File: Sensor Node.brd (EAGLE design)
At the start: 30.5 x 59.7 mm, 31 parts, among them Q1 IRLML6402, U1 ATMEGA328P_TQFP, X16 16MHZ, X8 8MHZ

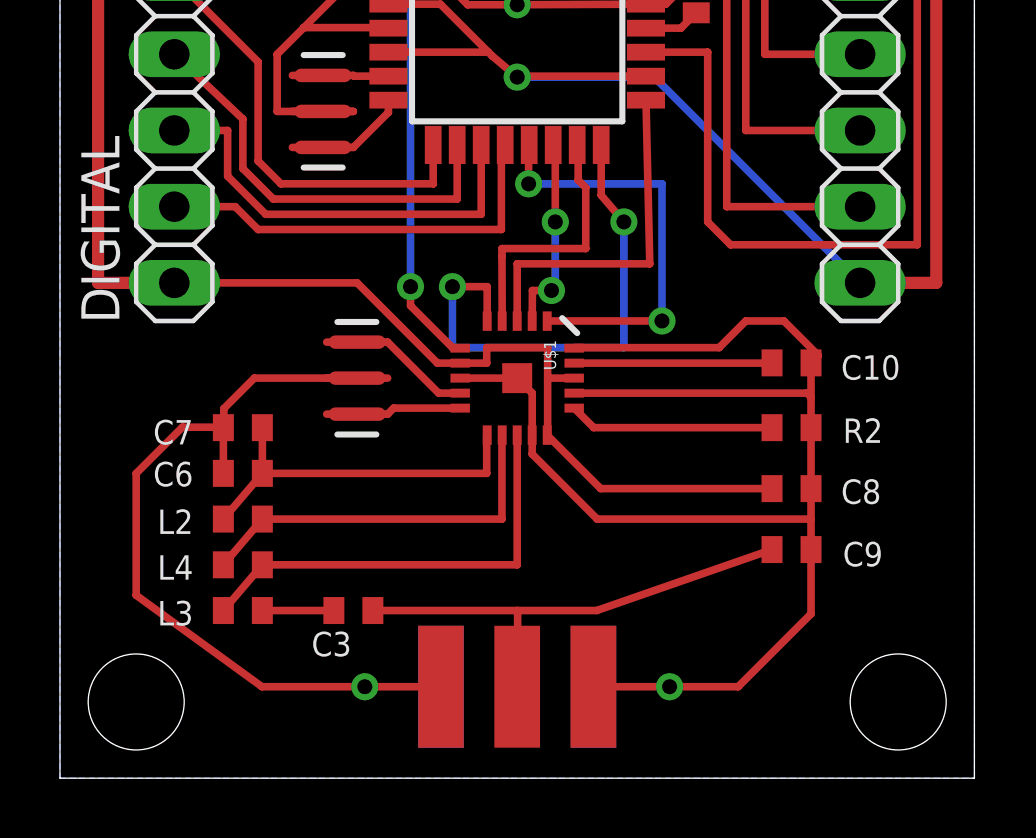
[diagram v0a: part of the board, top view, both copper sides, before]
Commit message: Distance optimization
Reduce the distance between the RF components
Make vias round
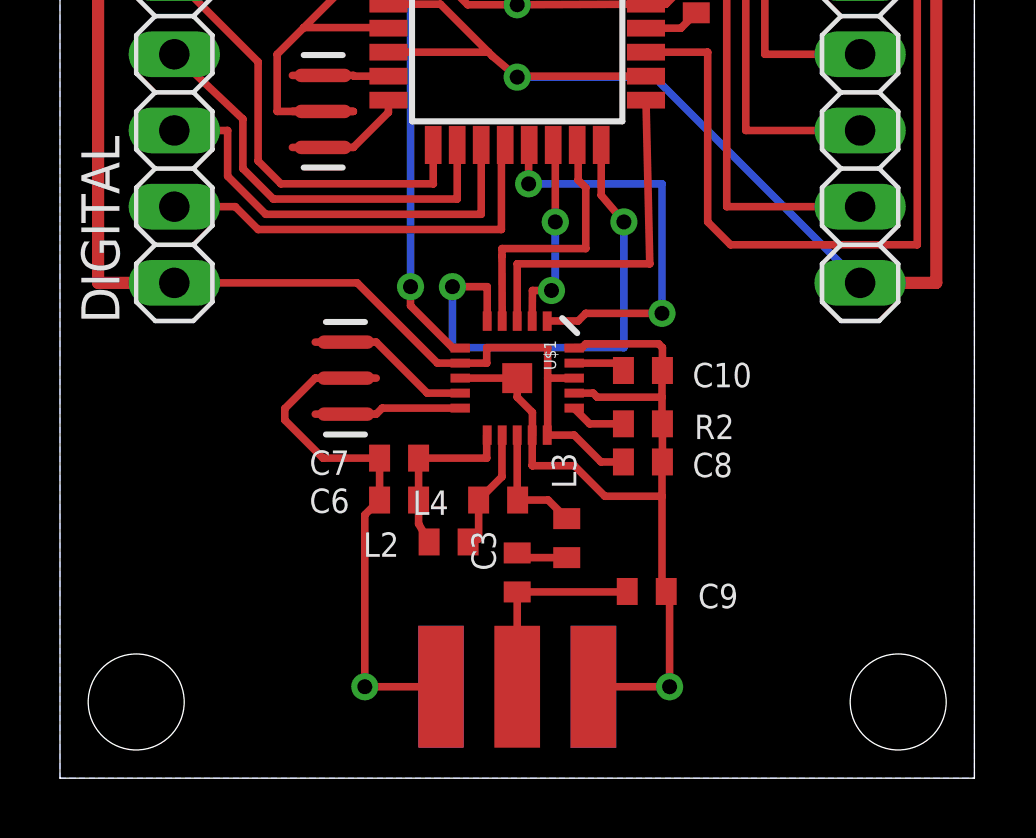
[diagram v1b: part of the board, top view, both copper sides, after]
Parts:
- moved L3 11.1 mm to (16.9, 8.00), turned to 270 degrees
- moved L4 8.78 mm to (14.6, 9.27)
- moved L2 6.90 mm to (13.0, 7.87)
- moved C3 5.61 mm to (15.2, 6.86), turned to 270 degrees
- moved C7 5.31 mm to (11.3, 10.7)
- moved C6 5.28 mm to (11.3, 9.27)
- moved C8 5.03 mm to (19.4, 10.5)
- moved C9 5.02 mm to (19.6, 6.22)
- moved C10 4.96 mm to (19.4, 13.6)
- moved R2 4.95 mm to (19.4, 11.8)
- moved X16 0.38 mm to (9.53, 13.3)
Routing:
- net GND: track 175.2 -> 146.5 mm
- net N$6: track 14.8 -> 4.06 mm
- net N$12: track 17.2 -> 7.32 mm
- net N$10: track 12.8 -> 4.16 mm
- net N$14: track 12.3 -> 5.94 mm
- net VCC: track 174.3 -> 169.0 mm
- net N$11: track 6.86 -> 1.86 mm
- net N$13: track 6.60 -> 1.74 mm
- net N$3: track 2.38 -> 1.72 mm

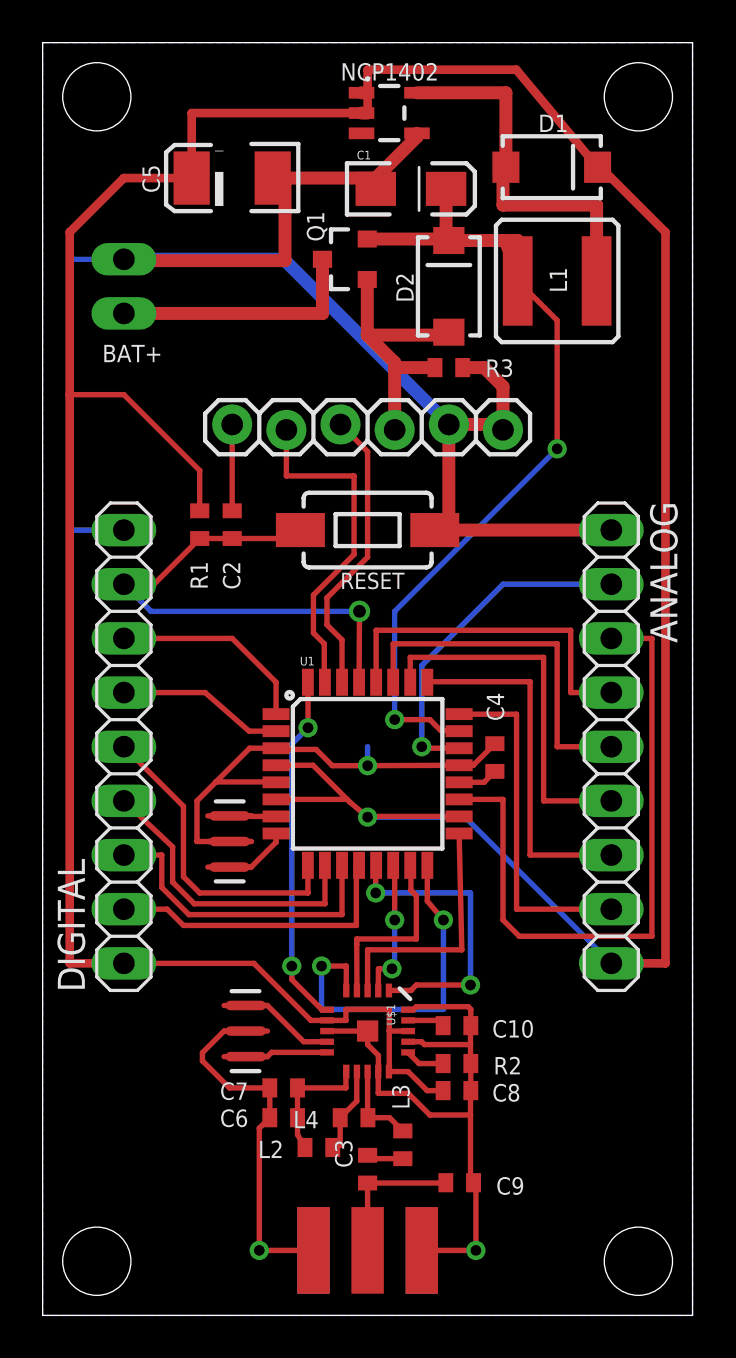
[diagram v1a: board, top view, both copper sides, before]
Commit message: Refactoring
Replace the FTDI pinheader
Remove unwanted text
Move and resize text
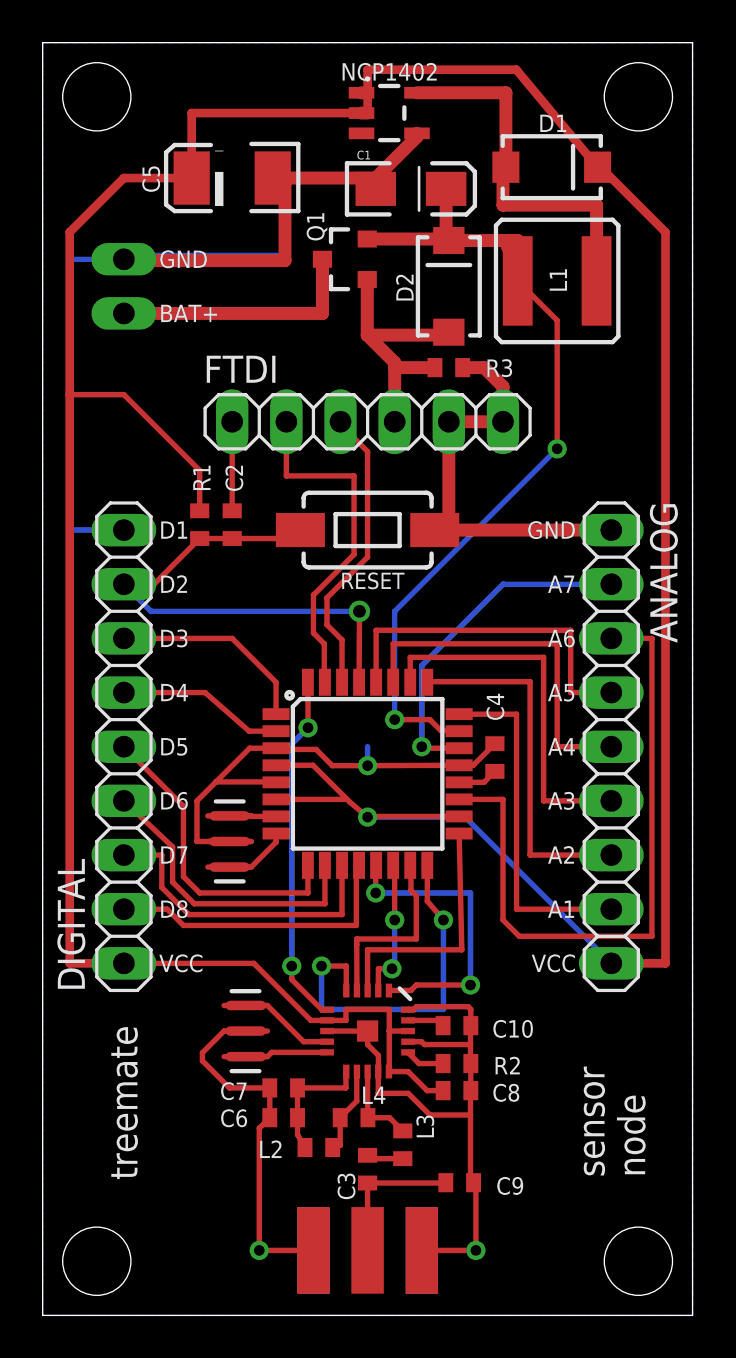
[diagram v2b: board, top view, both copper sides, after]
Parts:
- FTDI: device SparkFun-Connectors:1X06_LOCK -> pinhead:1X06
- moved FTDI 6.35 mm to (15.2, 41.9)
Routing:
- net GND: track 146.5 -> 135.2 mm
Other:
- board text added: "A1"
- board text added: "A2"
- board text added: "A3"
- board text added: "A4"
- board text added: "A5"
- board text added: "A6"
- board text added: "A7"
- board text added: "D1"
- board text added: "D2"
- board text added: "D3"
- board text added: "D4"
- board text added: "D5"
- board text added: "D6"
- board text added: "D7"
- board text added: "D8"
- board text added: "GND"
- board text added: "VCC"
- board text added: "sensor node"
- board text added: "treemate"
- board text removed: "treemate/sensor_node"
